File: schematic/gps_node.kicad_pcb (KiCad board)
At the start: 2 copper layers, 48 x 75 mm, 69 parts, among them IC1 MCP73831/2, J1 Mounting Hole, J11 AVR ICSP, J12 UART RF, J13 LIPO_BAT, J14 SOLAR, J15 UART GPS, J16 FW_UPDATE, J17 u.FL connector, J2 Mounting Hole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

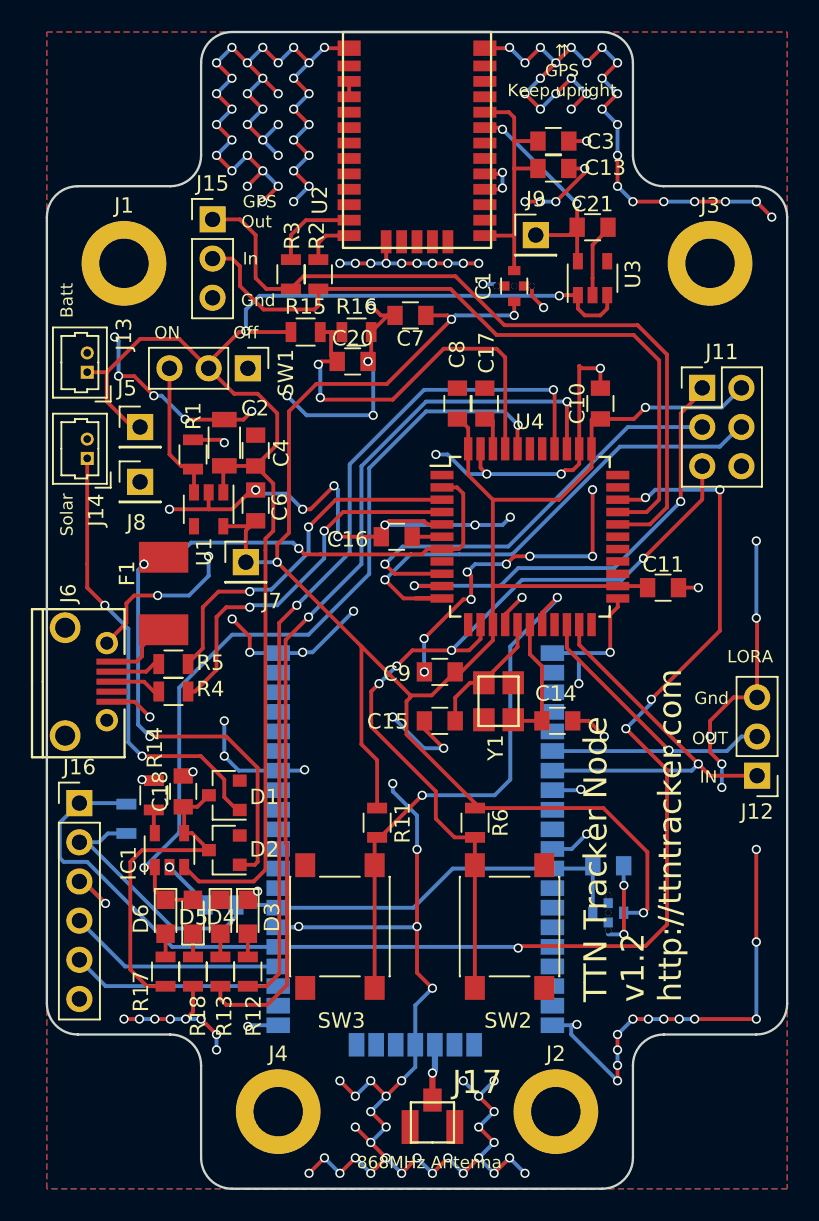
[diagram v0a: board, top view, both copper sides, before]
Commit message: Fix miso/mosi
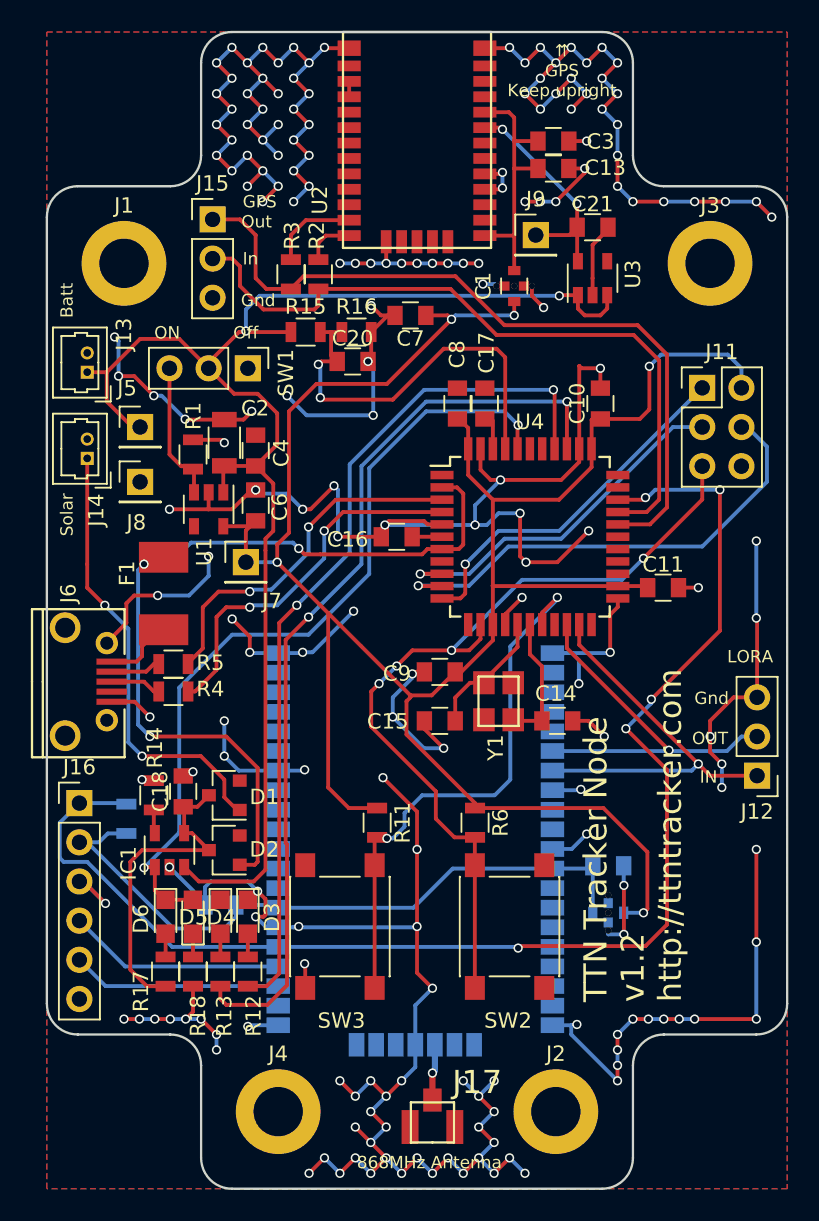
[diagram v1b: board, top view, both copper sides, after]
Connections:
- U4 pad 10: /MISO -> /MOSI
- U4 pad 11: /MOSI -> /MISO
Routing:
- net +3V3: track 140.0 -> 148.3 mm
- net /MISO: track 29.3 -> 23.9 mm, vias 2 -> 1
- net /SCK: track 28.2 -> 23.7 mm
- net GND: track 437.6 -> 441.4 mm, vias 201 -> 196
- net /MOSI: track 33.1 -> 31.5 mm
- net /BUTTON_1: track 35.3 -> 36.0 mm

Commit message: Decrease islands
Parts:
- moved C5 1.09 mm to (111.9, 116.7), turned to 90 degrees
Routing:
- net GND: track 441.4 -> 434.2 mm, vias 196 -> 193
- net /charge_status: track 52.9 -> 47.7 mm
- net /LED_OUT_GRN: track 59.7 -> 54.9 mm
- net /LED_OUT_RED: track 56.4 -> 52.8 mm
- net /USBD+: track 24.3 -> 21.3 mm
- net /BUTTON_1: track 36.0 -> 33.2 mm
- net /USBD-: track 23.4 -> 20.9 mm
- net /V_Charger: track 20.9 -> 18.5 mm
- net VBUS: track 55.0 -> 56.3 mm
- net /V_RN: track 44.2 -> 43.3 mm
- net +3V3: track 148.3 -> 147.4 mm
- net /V_Solar: track 29.2 -> 29.9 mm

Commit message: Fixed minor silkscreen issues
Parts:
- moved D1 3.05 mm to (111.5, 107.4)
- moved R14 3.05 mm to (106.9, 107.4)
- moved C18 2.80 mm to (109.0, 107.4)
- moved D2 2.79 mm to (111.5, 111.3)
- moved IC1 2.54 mm to (108.0, 111.5)
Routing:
- net VBUS: track 56.3 -> 51.4 mm
- net /V_Charger: track 18.5 -> 22.0 mm
- net +BATT: track 94.4 -> 91.3 mm
- net /charge_status: track 47.7 -> 50.3 mm
- net /V_Solar: track 29.9 -> 28.1 mm
- net GND: track 434.2 -> 432.7 mm, vias 193 -> 190
- net Net-(IC1-Pad5): track 1.53 -> 2.04 mm
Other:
- board text added: "+BATT"
- board text added: "3.3v"
- board text added: "GND"
- board text added: "RESET"
- board text added: "USER"
- board text added: "V_bak"
